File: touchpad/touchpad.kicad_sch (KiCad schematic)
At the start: 20 parts, among them J1 Conn_01x22, J10 Conn_01x01, J11 Conn_01x01, J12 Conn_01x01, J13 Conn_01x01, J14 Conn_01x01, J15 Conn_01x01, J16 Conn_01x01, J2 Conn_01x22, J3 Conn_01x01, J4 Conn_01x01, J5 Conn_01x01, J6 Conn_01x01, J7 Conn_01x01, J8 Conn_01x01, J9 Conn_01x01

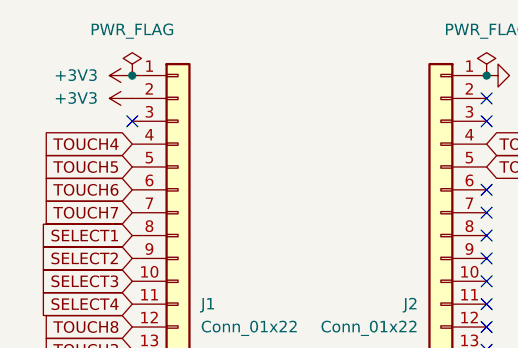
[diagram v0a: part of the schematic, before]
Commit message: Delete +3V3 from 4 dev boards
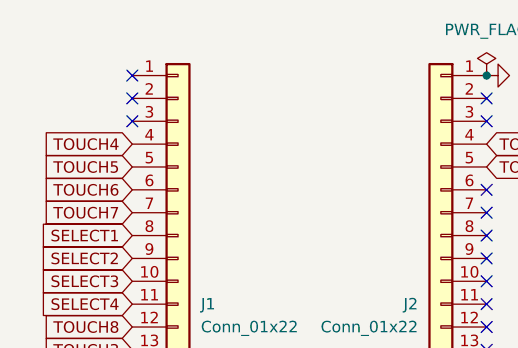
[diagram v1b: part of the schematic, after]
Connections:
- net +3V3: no longer names the net of J1.1 (Pin_1)
- net +3V3: no longer J1.2 (Pin_2)
- no-connect marks 28 -> 30
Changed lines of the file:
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@@
 	(paper "A4")
 	(junction
-		(at 49.53 66.04)
-		(diameter 0)
-		(color 0 0 0 0)
-	)
-	(junction
 		(at 88.9 66.04)
 		(diameter 0)
@@
 	)
 	(no_connect
+		(at 49.53 66.04)
+	)
+	(no_connect
 		(at 88.9 96.52)
 	)
+	(no_connect
+		(at 49.53 68.58)
+	)
 	(global_label "TOUCH1"
 		(shape input)
@@
 	)
 	(symbol
-		(lib_id "power:+3V3")
-		(at 49.53 66.04 90)
-		(unit 1)
-		(exclude_from_sim no)
-		(in_bom yes)
-		(on_board yes)
-		(dnp no)
-		(fields_autoplaced yes)
-		(property "Reference" "#PWR01"
-			(at 53.34 66.04 0)
-			(effects
-				(font
-					(size 1.27 1.27)
-				)
-				(hide yes)
-			)
-		)
-		(property "Value" "+3V3"
-			(at 45.72 66.0399 90)
-			(effects
-				(font
-					(size 1.27 1.27)
-				)
-				(justify left)
-			)
-		)
-		(property "Footprint" ""
-			(at 49.53 66.04 0)
-			(effects
-				(font
-					(size 1.27 1.27)
-				)
-				(hide yes)
-			)
-		)
-		(property "Datasheet" ""
-			(at 49.53 66.04 0)
-			(effects
-				(font
-					(size 1.27 1.27)
-				)
-				(hide yes)
-			)
-		)
-		(property "Description" "Power symbol creates a global label with name \"+3V3\""
-			(at 49.53 66.04 0)
-			(effects
-				(font
-					(size 1.27 1.27)
-				)
-				(hide yes)
-			)
-		)
-		(pin "1"
-		)
-		(instances
-			(project "touchpad"
-				(path "/2bdd9136-a122-406d-a063-905c75ab81be"
-					(reference "#PWR01")
-					(unit 1)
-				)
-			)
-		)
-	)
-	(symbol
 		(lib_id "SKRPACE010:SKRPACE010")
 		(at 241.3 74.93 0)
@@
 	)
 	(symbol
-		(lib_id "power:+3V3")
-		(at 49.53 68.58 90)
-		(unit 1)
-		(exclude_from_sim no)
-		(in_bom yes)
-		(on_board yes)
-		(dnp no)
-		(fields_autoplaced yes)
-		(property "Reference" "#PWR02"
-			(at 53.34 68.58 0)
-			(effects
-				(font
-					(size 1.27 1.27)
-				)
-				(hide yes)
-			)
-		)
-		(property "Value" "+3V3"
-			(at 45.72 68.5799 90)
-			(effects
-				(font
-					(size 1.27 1.27)
-				)
-				(justify left)
-			)
-		)
-		(property "Footprint" ""
-			(at 49.53 68.58 0)
-			(effects
-				(font
-					(size 1.27 1.27)
-				)
-				(hide yes)
-			)
-		)
-		(property "Datasheet" ""
-			(at 49.53 68.58 0)
-			(effects
-				(font
-					(size 1.27 1.27)
-				)
-				(hide yes)
-			)
-		)
-		(property "Description" "Power symbol creates a global label with name \"+3V3\""
-			(at 49.53 68.58 0)
-			(effects
-				(font
-					(size 1.27 1.27)
-				)
-				(hide yes)
-			)
-		)
-		(pin "1"
-		)
-		(instances
-			(project "touchpad"
-				(path "/2bdd9136-a122-406d-a063-905c75ab81be"
-					(reference "#PWR02")
-					(unit 1)
-				)
-			)
-		)
-	)
-	(symbol
 		(lib_id "Connector_Generic:Conn_01x01")
 		(at 162.56 86.36 270)
@@
 					(unit 1)
 				)
-			)
-		)
-	)
-	(symbol
-		(lib_id "power:PWR_FLAG")
-		(at 49.53 66.04 0)
-		(unit 1)
-		(exclude_from_sim no)
-		(in_bom yes)
-		(on_board yes)
-		(dnp no)
-		(fields_autoplaced yes)
-		(property "Reference" "#FLG01"
-			(at 49.53 64.135 0)
-			(effects
-				(font
-					(size 1.27 1.27)
-				)
-				(hide yes)
-			)
-		)
-		(property "Value" "PWR_FLAG"
-			(at 49.53 60.96 0)
-			(effects
-				(font
-					(size 1.27 1.27)
-				)
-			)
-		)
-		(property "Footprint" ""
-			(at 49.53 66.04 0)
-			(effects
-				(font
-					(size 1.27 1.27)
-				)
-				(hide yes)
-			)
-		)
-		(property "Datasheet" "~"
-			(at 49.53 66.04 0)
-			(effects
-				(font
-					(size 1.27 1.27)
-				)
-				(hide yes)
-			)
-		)
-		(property "Description" "Special symbol for telling ERC where power comes from"
-			(at 49.53 66.04 0)
-			(effects
-				(font
-					(size 1.27 1.27)
-				)
-				(hide yes)
-			)
-		)
-		(pin "1"
-		)
-		(instances
-			(project "touchpad"
-				(path "/2bdd9136-a122-406d-a063-905c75ab81be"
-					(reference "#FLG01")
-					(unit 1)
-				)
